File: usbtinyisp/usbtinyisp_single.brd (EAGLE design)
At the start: 44 x 36 mm, 27 parts, among them IC1 ATTINY2313-20P, IC2 74LVX125D, Q1 12000

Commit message: replace elko package
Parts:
- C2: device rcl:E2,5-7 -> rcl:E2,5-6
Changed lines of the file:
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@@
 <layer number="23" name="tOrigins" color="15" fill="1" visible="yes" active="yes"/>
 <layer number="24" name="bOrigins" color="15" fill="1" visible="yes" active="yes"/>
-<layer number="25" name="tNames" color="7" fill="1" visible="no" active="yes"/>
-<layer number="26" name="bNames" color="7" fill="1" visible="no" active="yes"/>
+<layer number="25" name="tNames" color="7" fill="1" visible="yes" active="yes"/>
+<layer number="26" name="bNames" color="7" fill="1" visible="yes" active="yes"/>
 <layer number="27" name="tValues" color="7" fill="1" visible="no" active="yes"/>
 <layer number="28" name="bValues" color="7" fill="1" visible="no" active="yes"/>
@@
 <element name="X1" library="con-berg-ez" package="PN61729" value="" x="3" y="18" rot="R270"/>
 <element name="IC2" library="74xx-eu" package="SO14" value="74LVX125D" x="16.51" y="11.43" rot="MR270"/>
-<element name="C2" library="rcl" package="E2,5-7" value="100u" x="15.875" y="4.445" rot="R270"/>
+<element name="C2" library="rcl" package="E2,5-6" value="100u" x="15.875" y="4.445" rot="R270"/>
 <element name="U$1" library="holes" package="3,2-PAD" value="" x="4" y="4"/>
 <element name="U$2" library="holes" package="3,2-PAD" value="" x="40" y="4"/>

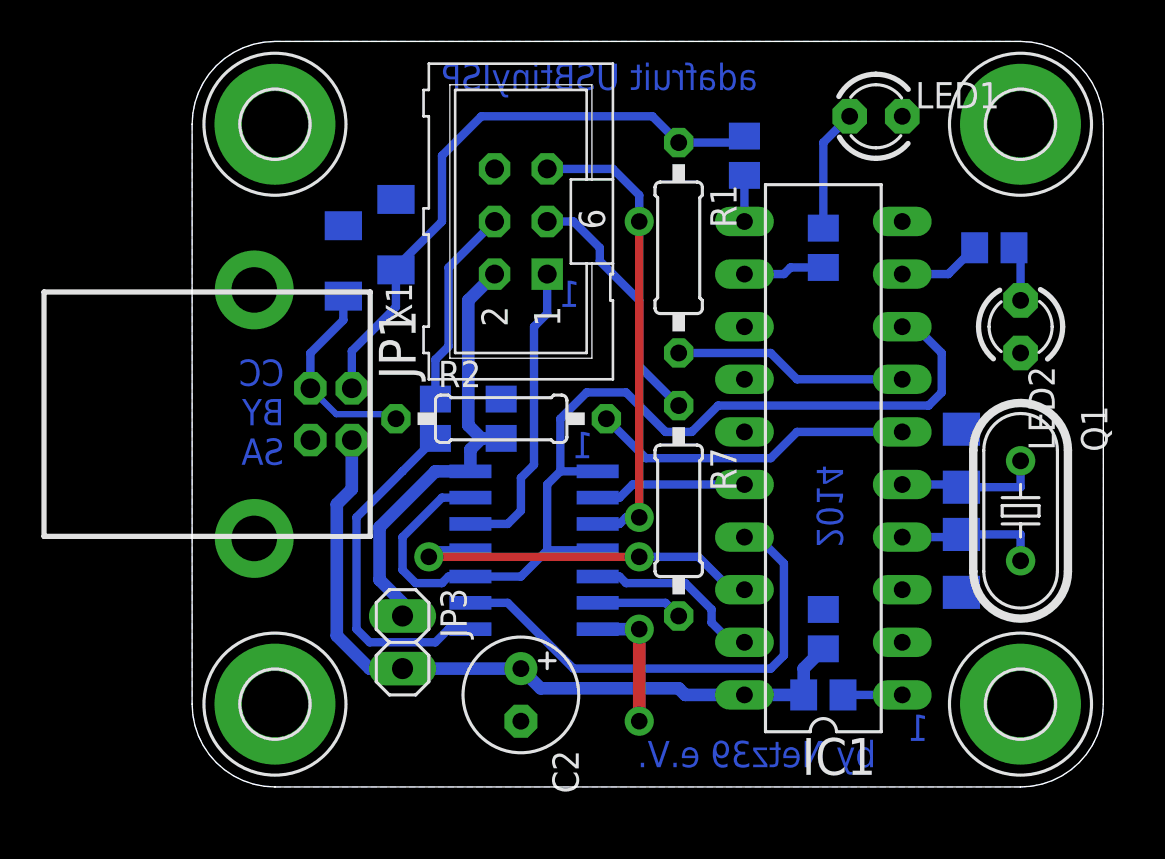
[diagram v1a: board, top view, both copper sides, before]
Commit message: move vias for round wire lengths
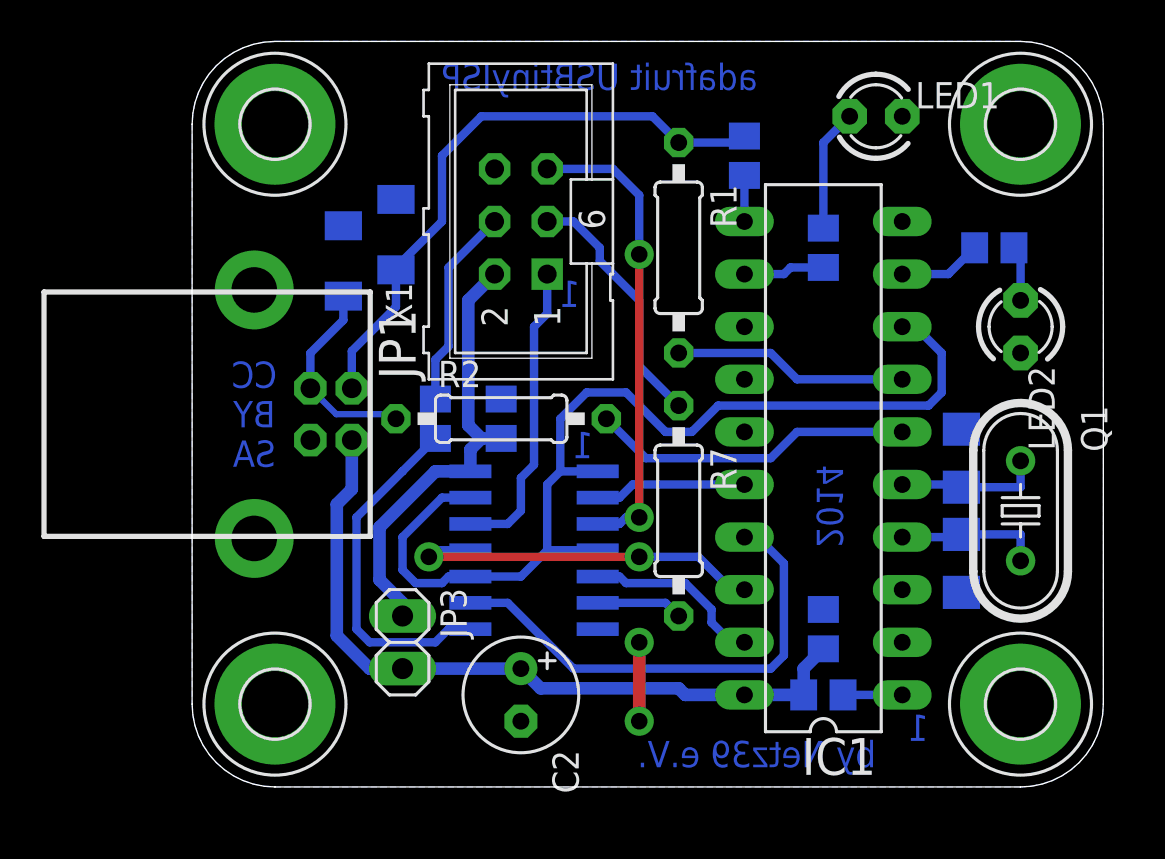
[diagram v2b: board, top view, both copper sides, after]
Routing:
- net GND: track 6.45 -> 3.81 mm
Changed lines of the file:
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@@
 <setting verticaltext="up"/>
 </settings>
-<grid distance="25" unitdist="mil" unit="mil" style="dots" multiple="1" display="no" altdistance="12.5" altunitdist="mil" altunit="mil"/>
+<grid distance="50" unitdist="mil" unit="mil" style="dots" multiple="1" display="yes" altdistance="25" altunitdist="mil" altunit="mil"/>
 <layers>
 <layer number="1" name="Top" color="4" fill="1" visible="yes" active="yes"/>
@@
 <text x="27.305" y="33.655" size="1.27" layer="16" font="vector" ratio="15" rot="MR0">adafruit USBtinyISP</text>
 <text x="31.4325" y="15.5575" size="1.27" layer="16" font="vector" ratio="15" rot="MR270">2014</text>
-<text x="4.445" y="15.5575" size="1.27" layer="16" font="vector" ratio="15" rot="MR0">CC
+<text x="3" y="18" size="1.27" layer="16" font="vector" ratio="15" rot="MR0" align="center">CC
 BY
 SA</text>
@@
 <vertex x="0" y="32"/>
 </polygon>
-<via x="21.59" y="7.62" extent="1-16" drill="0.8" shape="square"/>
-<wire x1="21.59" y1="7.62" x2="21.59" y2="3.175" width="0.6096" layer="1"/>
+<via x="21.59" y="6.985" extent="1-16" drill="0.8" shape="square"/>
+<wire x1="21.59" y1="6.985" x2="21.59" y2="3.175" width="0.6096" layer="1"/>
 <via x="21.59" y="3.175" extent="1-16" drill="0.8" shape="square"/>
-<wire x1="19.5834" y1="7.62" x2="21.59" y2="7.62" width="0.6096" layer="16"/>
 <contactref element="C5" pad="2"/>
 <contactref element="LED1" pad="K"/>
@@
 <contactref element="IC2" pad="3"/>
 <via x="21.59" y="13.0175" extent="1-16" drill="0.8" shape="octagon"/>
-<wire x1="21.59" y1="13.0175" x2="21.59" y2="27.305" width="0.4064" layer="1"/>
-<via x="21.59" y="27.305" extent="1-16" drill="0.8" shape="octagon"/>
+<wire x1="21.59" y1="13.0175" x2="21.59" y2="25.7175" width="0.4064" layer="1"/>
+<via x="21.59" y="25.7175" extent="1-16" drill="0.8" shape="octagon"/>
 <wire x1="19.5834" y1="12.7" x2="20.6375" y2="12.7" width="0.4064" layer="16"/>
 <wire x1="20.6375" y1="12.7" x2="20.955" y2="13.0175" width="0.4064" layer="16"/>
 <wire x1="20.955" y1="13.0175" x2="21.59" y2="13.0175" width="0.4064" layer="16"/>
-<wire x1="21.59" y1="27.305" x2="21.59" y2="28.575" width="0.4064" layer="16"/>
+<wire x1="21.59" y1="25.7175" x2="21.59" y2="28.575" width="0.4064" layer="16"/>
 <wire x1="21.59" y1="28.575" x2="20.32" y2="29.845" width="0.4064" layer="16"/>
 <wire x1="20.32" y1="29.845" x2="17.145" y2="29.845" width="0.4064" layer="16"/>
